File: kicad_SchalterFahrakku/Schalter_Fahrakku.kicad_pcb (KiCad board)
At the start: 2 copper layers, 10 parts, among them P3 uC_IN, Q1 IRLML6344, Q2 IPD90P03

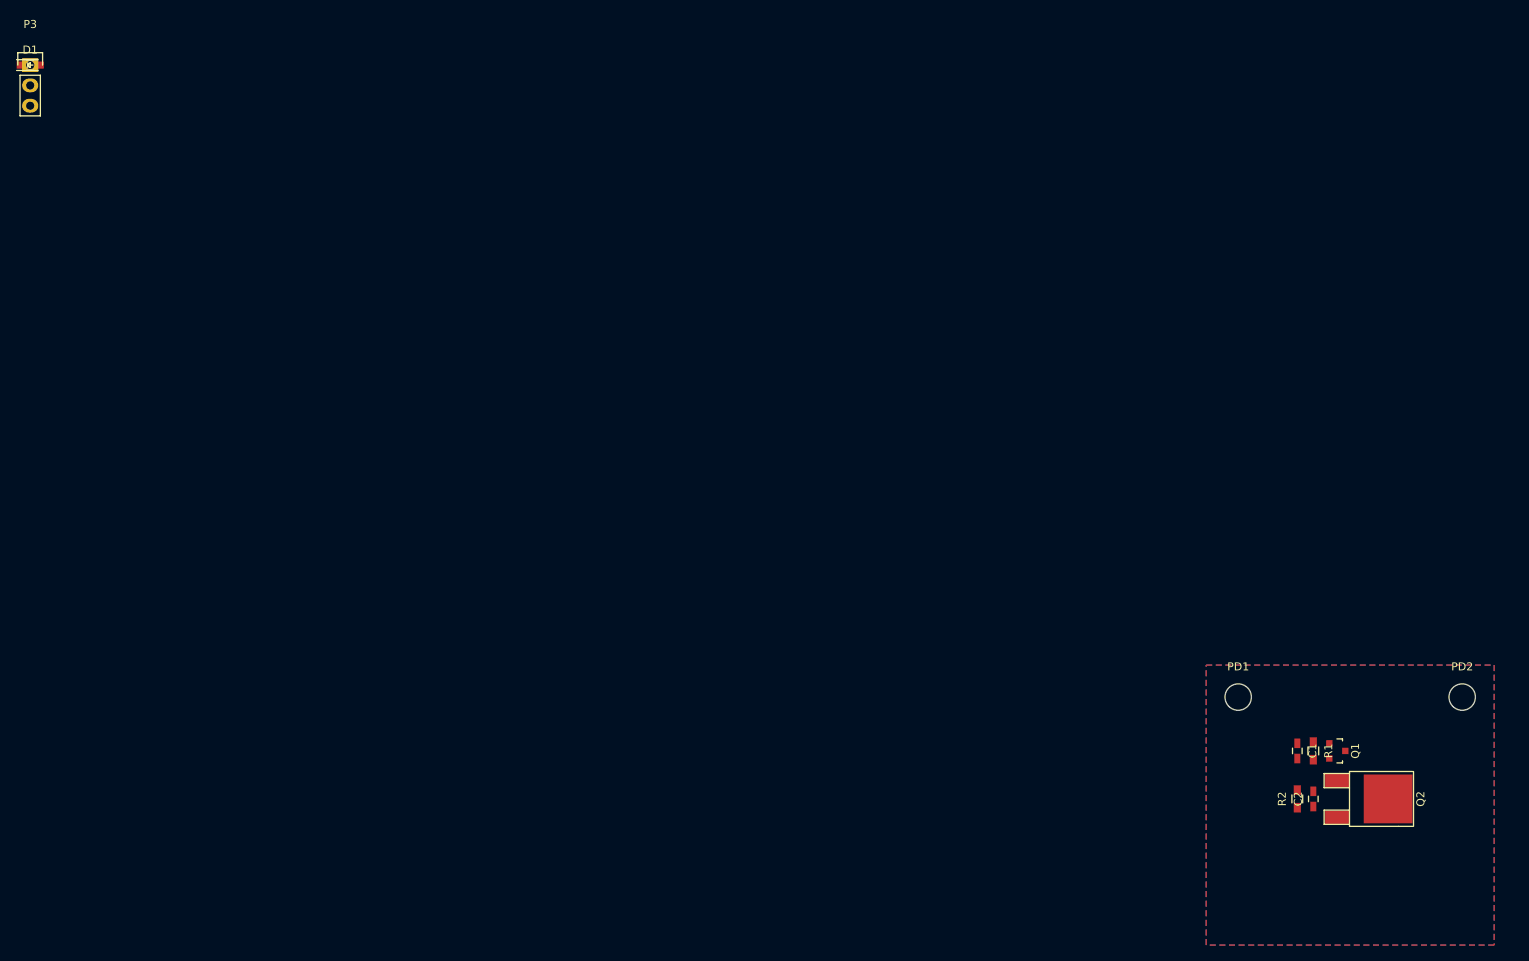
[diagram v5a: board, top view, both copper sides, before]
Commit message: - 5V_Servo Zusätzlich zur verfügung gestellt - Footprints für Pinleisten mit Verrigelung Hinzugefügt
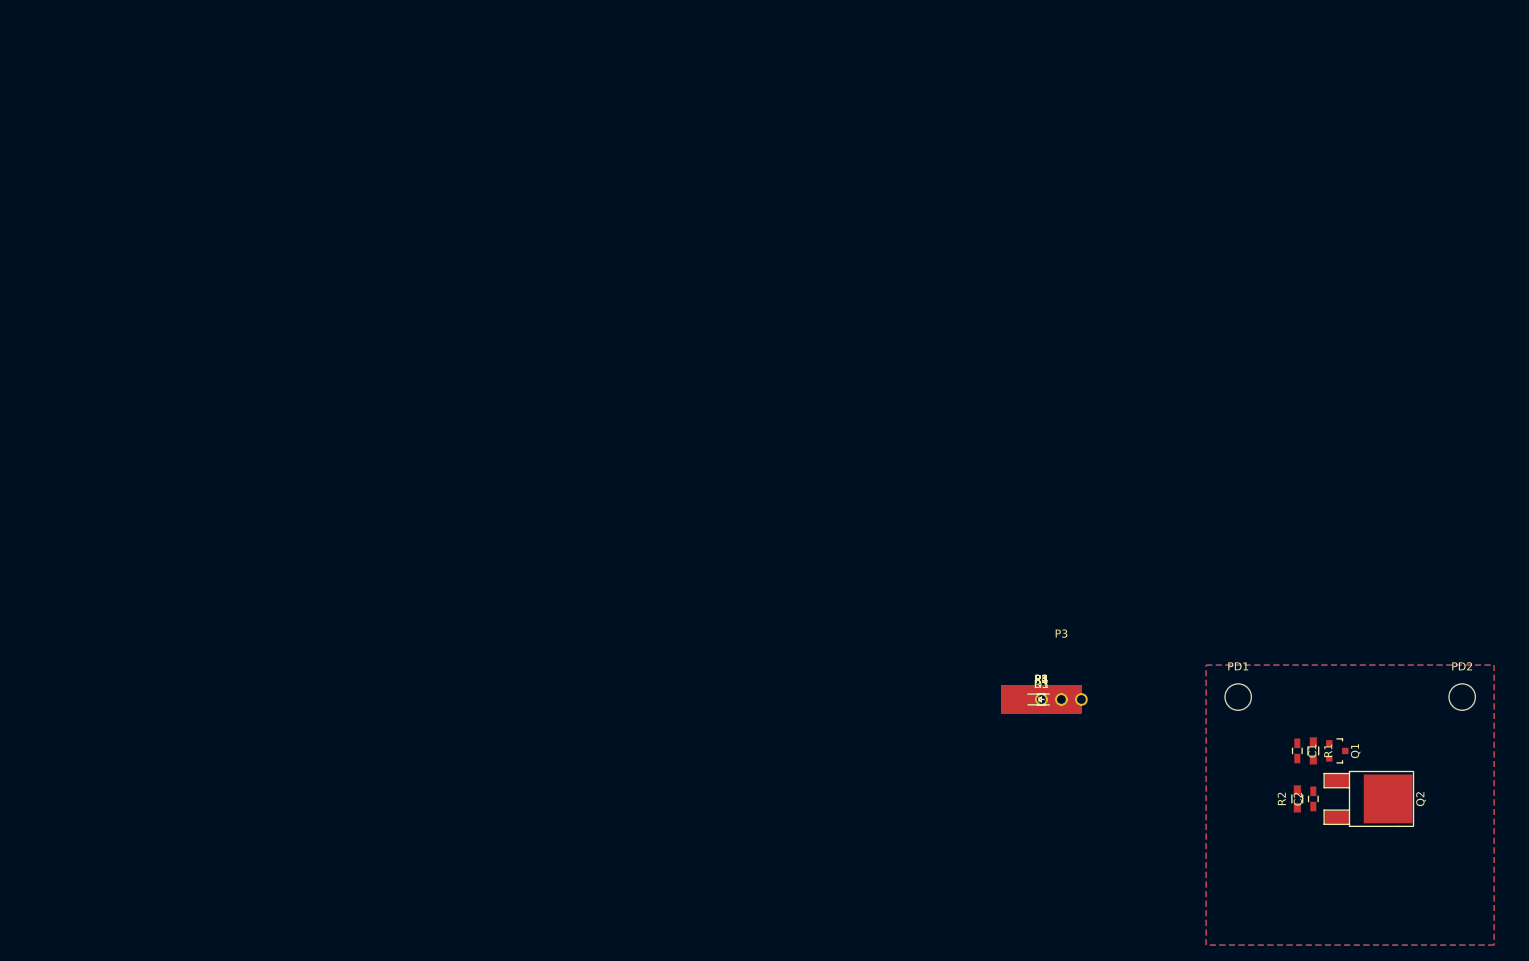
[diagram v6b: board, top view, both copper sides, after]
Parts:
- added P1: V_IN+, Custom:Pad_SMD_3.5x10, F.Cu at (126.4, 79.3)
- added P2: V_IN-, Custom:Pad_SMD_3.5x10, F.Cu at (126.4, 79.3)
- added P4, P5: V_OUT+, Custom:Pad_SMD_3.5x10, F.Cu at (126.4, 79.3)
- added R3: 3k6, Resistors_SMD:R_0603_HandSoldering, F.Cu at (126.4, 79.3)
- P3: footprint Pin_Headers:Pin_Header_Straight_1x03 -> Custom:PS25_3W_BR
- moved D1 149.2 mm to (126.4, 79.3)
- moved P3 149.2 mm to (126.4, 79.3)
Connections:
- D1 pad 2: (no net) -> Net-(D1-Pad2)
- Q2 pad 2: (no net) -> Net-(P4-Pad1)
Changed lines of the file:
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@@
 (kicad_pcb (version 4) (host pcbnew 4.0.2-stable)
   (general
-    (links 15)
-    (no_connects 13)
+    (links 19)
+    (no_connects 11)
     (area 0 0 0 0)
     (thickness 1.6)
@@
     (tracks 0)
     (zones 0)
-    (modules 10)
-    (nets 5)
+    (modules 15)
+    (nets 7)
   )
   (page A4)
@@
   (net 3 "Net-(C2-Pad1)")
   (net 4 "Net-(C2-Pad2)")
+  (net 5 "Net-(D1-Pad2)")
+  (net 6 "Net-(P4-Pad1)")
   (net_class Default "Dies ist die voreingestellte Netzklasse."
     (clearance 0.2)
@@
     (add_net "Net-(C2-Pad1)")
     (add_net "Net-(C2-Pad2)")
+    (add_net "Net-(D1-Pad2)")
+    (add_net "Net-(P4-Pad1)")
   )
   (module Capacitors_SMD:C_0603_HandSoldering (layer F.Cu)
@@
     (pad 1 smd rect (at -2.286 0 270) (size 1.651 3.048) (layers F.Cu F.Paste F.Mask)
       (net 4 "Net-(C2-Pad2)"))
-    (pad 2 smd rect (at 0 -6.35 270) (size 6.096 6.096) (layers F.Cu F.Paste F.Mask))
+    (pad 2 smd rect (at 0 -6.35 270) (size 6.096 6.096) (layers F.Cu F.Paste F.Mask)
+      (net 6 "Net-(P4-Pad1)"))
     (pad 3 smd rect (at 2.286 0 270) (size 1.651 3.048) (layers F.Cu F.Paste F.Mask)
       (net 3 "Net-(C2-Pad1)"))
@@
   )
   (module Custom:LED_0603_HandSoldering (layer F.Cu)
-    (at 0 0)
+    (at 126.4 79.3)
     (descr "Resistor SMD 0603, hand soldering")
     (tags "resistor 0603")
@@
     (pad 1 smd rect (at -1.1 0) (size 1.2 0.9) (layers F.Cu F.Paste F.Mask)
       (net 2 GND))
-    (pad 2 smd rect (at 1.1 0) (size 1.2 0.9) (layers F.Cu F.Paste F.Mask))
+    (pad 2 smd rect (at 1.1 0) (size 1.2 0.9) (layers F.Cu F.Paste F.Mask)
+      (net 5 "Net-(D1-Pad2)"))
     (model Resistors_SMD.3dshapes/R_0603_HandSoldering.wrl
       (at (xyz 0 0 0))
@@
     )
   )
-  (module Pin_Headers:Pin_Header_Straight_1x03 (layer F.Cu)
-    (at 0 0)
-    (descr "Through hole pin header")
-    (tags "pin header")
-    (fp_text reference P3 (at 0 -5.1) (layer F.SilkS)
-      (effects (font (size 1 1) (thickness 0.15)))
-    )
-    (fp_text value uC_IN (at 0 -3.1) (layer F.Fab)
-      (effects (font (size 1 1) (thickness 0.15)))
-    )
-    (fp_line (start -1.75 -1.75) (end -1.75 6.85) (layer F.CrtYd) (width 0.05))
-    (fp_line (start 1.75 -1.75) (end 1.75 6.85) (layer F.CrtYd) (width 0.05))
-    (fp_line (start -1.75 -1.75) (end 1.75 -1.75) (layer F.CrtYd) (width 0.05))
-    (fp_line (start -1.75 6.85) (end 1.75 6.85) (layer F.CrtYd) (width 0.05))
-    (fp_line (start -1.27 1.27) (end -1.27 6.35) (layer F.SilkS) (width 0.15))
-    (fp_line (start -1.27 6.35) (end 1.27 6.35) (layer F.SilkS) (width 0.15))
-    (fp_line (start 1.27 6.35) (end 1.27 1.27) (layer F.SilkS) (width 0.15))
-    (fp_line (start 1.55 -1.55) (end 1.55 0) (layer F.SilkS) (width 0.15))
-    (fp_line (start 1.27 1.27) (end -1.27 1.27) (layer F.SilkS) (width 0.15))
-    (fp_line (start -1.55 0) (end -1.55 -1.55) (layer F.SilkS) (width 0.15))
-    (fp_line (start -1.55 -1.55) (end 1.55 -1.55) (layer F.SilkS) (width 0.15))
-    (pad 1 thru_hole rect (at 0 0) (size 2.032 1.7272) (drill 1.016) (layers *.Cu *.Mask F.SilkS)
+  (module Custom:Pad_SMD_3.5x10 (layer F.Cu)
+    (at 126.4 79.3)
+    (fp_text reference P1 (at 0 -2.54 180) (layer F.SilkS)
+      (effects (font (size 1 1) (thickness 0.15)))
+    )
+    (fp_text value V_IN+ (at -0.0254 2.794) (layer F.Fab)
+      (effects (font (size 1 1) (thickness 0.15)))
+    )
+    (pad 1 smd rect (at 0 0) (size 10 3.5) (layers F.Cu F.Paste F.Mask)
       (net 3 "Net-(C2-Pad1)"))
-    (pad 2 thru_hole oval (at 0 2.54) (size 2.032 1.7272) (drill 1.016) (layers *.Cu *.Mask F.SilkS)
-      (net 2 GND))
-    (pad 3 thru_hole oval (at 0 5.08) (size 2.032 1.7272) (drill 1.016) (layers *.Cu *.Mask F.SilkS)
+  )
+  (module Custom:Pad_SMD_3.5x10 (layer F.Cu)
+    (at 126.4 79.3)
+    (fp_text reference P2 (at 0 -2.54 180) (layer F.SilkS)
+      (effects (font (size 1 1) (thickness 0.15)))
+    )
+    (fp_text value V_IN- (at -0.0254 2.794) (layer F.Fab)
+      (effects (font (size 1 1) (thickness 0.15)))
+    )
+    (pad 1 smd rect (at 0 0) (size 10 3.5) (layers F.Cu F.Paste F.Mask)
+      (net 2 GND))
+  )
+  (module Custom:PS25_3W_BR (layer F.Cu)
+    (at 126.4 79.3)
+    (fp_text reference P3 (at 2.5 -8.2) (layer F.SilkS)
+      (effects (font (size 1 1) (thickness 0.15)))
+    )
+    (fp_text value uC_IN (at 2.5 3.3) (layer F.Fab)
+      (effects (font (size 1 1) (thickness 0.15)))
+    )
+    (fp_line (start 6.5 -7.35) (end 6.5 -2.35) (layer F.CrtYd) (width 0.15))
+    (fp_line (start -1.5 -7.35) (end 6.5 -7.35) (layer F.CrtYd) (width 0.15))
+    (fp_line (start -1.5 -2.35) (end -1.5 -7.35) (layer F.CrtYd) (width 0.15))
+    (fp_line (start 6.5 2.35) (end -1.5 2.35) (layer F.CrtYd) (width 0.15))
+    (fp_line (start 6.5 -2.35) (end 6.5 2.35) (layer F.CrtYd) (width 0.15))
+    (fp_line (start -1.5 -2.35) (end 6.5 -2.35) (layer F.CrtYd) (width 0.15))
+    (fp_line (start -1.5 2.35) (end -1.5 -2.35) (layer F.CrtYd) (width 0.15))
+    (pad 1 thru_hole circle (at 0 0) (size 1.6 1.6) (drill 1.1) (layers *.Cu *.Mask F.SilkS)
+      (net 3 "Net-(C2-Pad1)"))
+    (pad 2 thru_hole circle (at 2.5 0) (size 1.6 1.6) (drill 1.1) (layers *.Cu *.Mask F.SilkS)
+      (net 2 GND))
+    (pad 3 thru_hole circle (at 5 0) (size 1.6 1.6) (drill 1.1) (layers *.Cu *.Mask F.SilkS)
       (net 1 /CTL_DRIVE))
-    (model Pin_Headers.3dshapes/Pin_Header_Straight_1x03.wrl
-      (at (xyz 0 -0.1 0))
-      (scale (xyz 1 1 1))
-      (rotate (xyz 0 0 90))
-    )
-  )
+  )
+  (module Custom:Pad_SMD_3.5x10 (layer F.Cu)
+    (at 126.4 79.3)
+    (fp_text reference P4 (at 0 -2.54 180) (layer F.SilkS)
+      (effects (font (size 1 1) (thickness 0.15)))
+    )
+    (fp_text value V_OUT+ (at -0.0254 2.794) (layer F.Fab)
+      (effects (font (size 1 1) (thickness 0.15)))
+    )
+    (pad 1 smd rect (at 0 0) (size 10 3.5) (layers F.Cu F.Paste F.Mask)
+      (net 6 "Net-(P4-Pad1)"))
+  )
+  (module Custom:Pad_SMD_3.5x10 (layer F.Cu)
+    (at 126.4 79.3)
+    (fp_text reference P5 (at 0 -2.54 180) (layer F.SilkS)
+      (effects (font (size 1 1) (thickness 0.15)))
+    )
+    (fp_text value V_OUT+ (at -0.0254 2.794) (layer F.Fab)
+      (effects (font (size 1 1) (thickness 0.15)))
+    )
+    (pad 1 smd rect (at 0 0) (size 10 3.5) (layers F.Cu F.Paste F.Mask)
+      (net 2 GND))
+  )
+  (module Resistors_SMD:R_0603_HandSoldering (layer F.Cu)
+    (at 126.4 79.3)
+    (descr "Resistor SMD 0603, hand soldering")
+    (tags "resistor 0603")
+    (attr smd)
+    (fp_text reference R3 (at 0 -1.9) (layer F.SilkS)
+      (effects (font (size 1 1) (thickness 0.15)))
+    )
+    (fp_text value 3k6 (at 0 1.9) (layer F.Fab)
+      (effects (font (size 1 1) (thickness 0.15)))
+    )
+    (fp_line (start -2 -0.8) (end 2 -0.8) (layer F.CrtYd) (width 0.05))
+    (fp_line (start -2 0.8) (end 2 0.8) (layer F.CrtYd) (width 0.05))
+    (fp_line (start -2 -0.8) (end -2 0.8) (layer F.CrtYd) (width 0.05))
+    (fp_line (start 2 -0.8) (end 2 0.8) (layer F.CrtYd) (width 0.05))
+    (fp_line (start 0.5 0.675) (end -0.5 0.675) (layer F.SilkS) (width 0.15))
+    (fp_line (start -0.5 -0.675) (end 0.5 -0.675) (layer F.SilkS) (width 0.15))
+    (pad 1 smd rect (at -1.1 0) (size 1.2 0.9) (layers F.Cu F.Paste F.Mask)
+      (net 6 "Net-(P4-Pad1)"))
+    (pad 2 smd rect (at 1.1 0) (size 1.2 0.9) (layers F.Cu F.Paste F.Mask)
+      (net 5 "Net-(D1-Pad2)"))
+    (model Resistors_SMD.3dshapes/R_0603_HandSoldering.wrl
+      (at (xyz 0 0 0))
+      (scale (xyz 1 1 1))
+      (rotate (xyz 0 0 0))
+    )
+  )

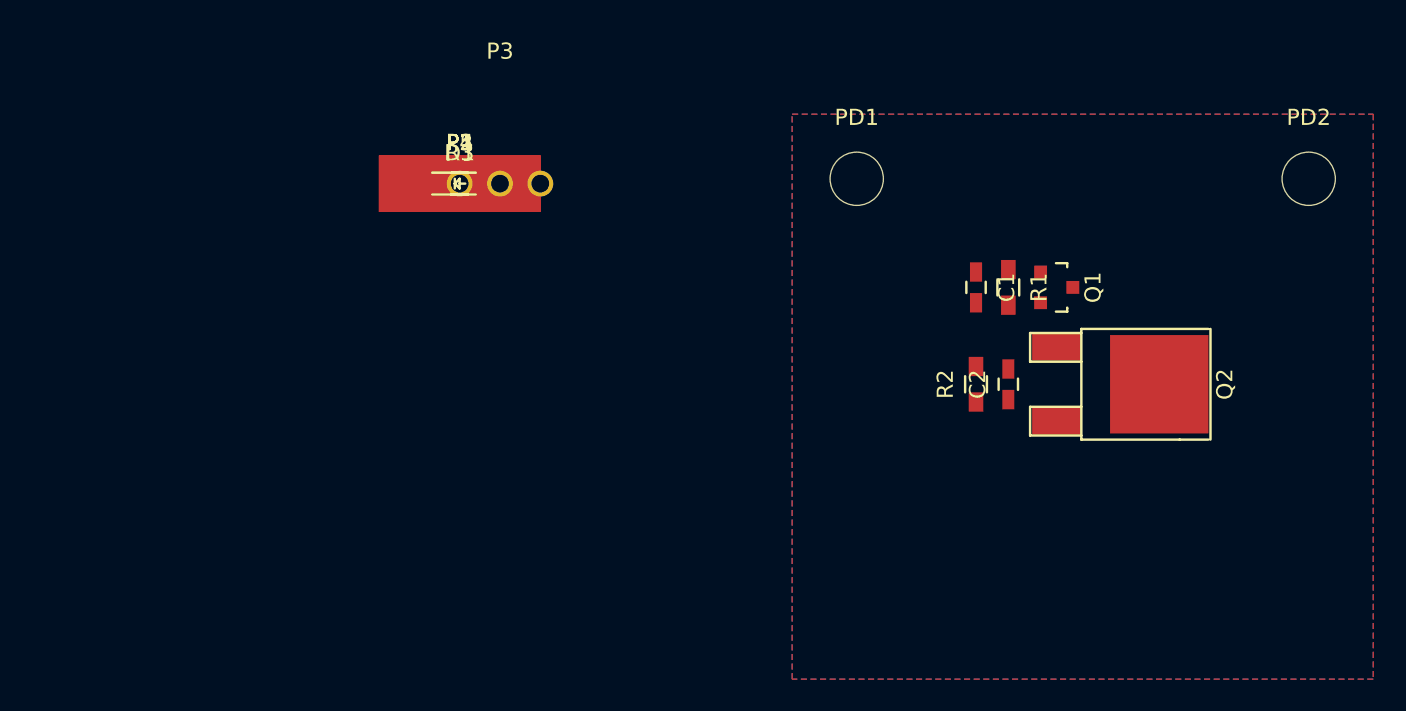
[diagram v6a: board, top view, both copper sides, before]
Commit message: - Layout Schalterplatine ohne Routing
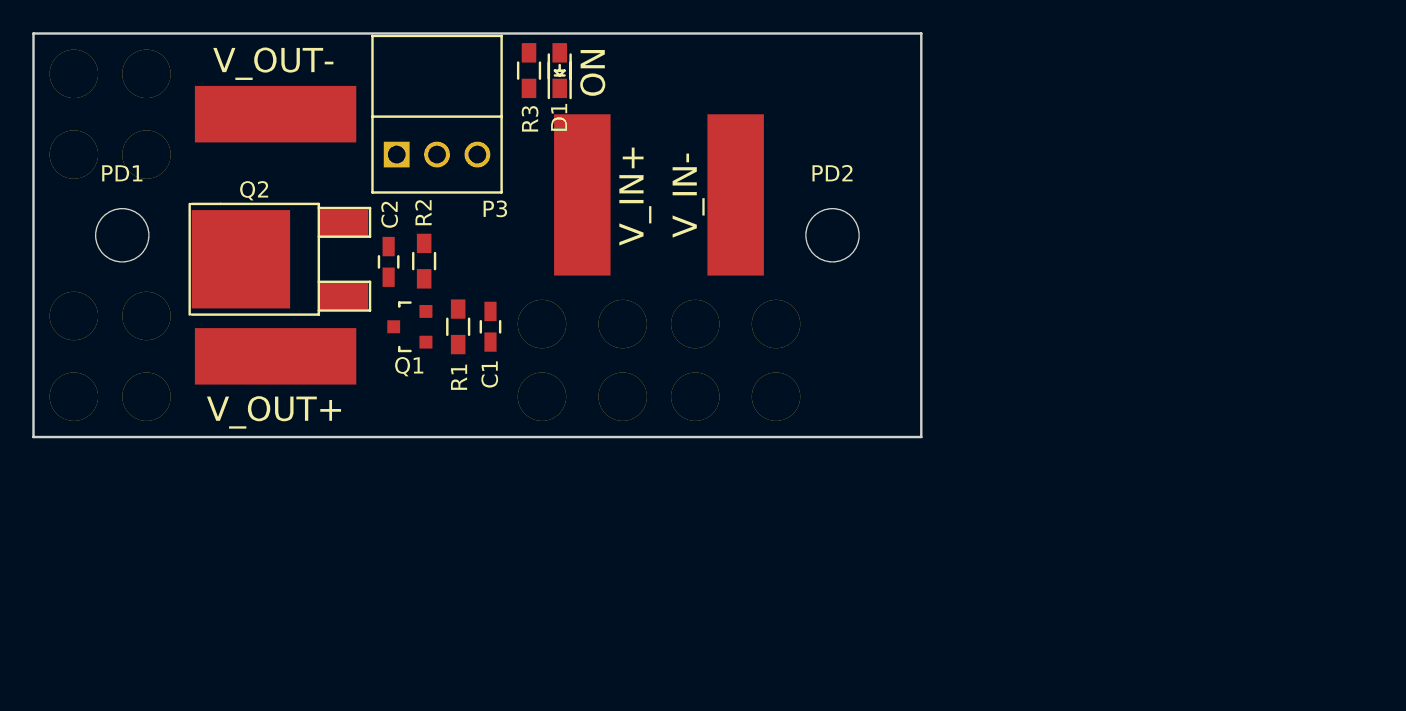
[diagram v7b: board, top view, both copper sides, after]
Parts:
- added PD10: Hole, Custom:Hole_3mm, F.Cu at (107.0, 72.5)
- added PD11: Hole, Custom:Hole_3mm, F.Cu at (131.5, 92.5)
- added PD12: Hole, Custom:Hole_3mm, F.Cu at (136.5, 92.5)
- added PD13: Hole, Custom:Hole_3mm, F.Cu at (131.5, 88.0)
- added PD14: Hole, Custom:Hole_3mm, F.Cu at (136.5, 88.0)
- added PD15: Hole, Custom:Hole_3mm, F.Cu at (146.0, 92.5)
- added PD16: Hole, Custom:Hole_3mm, F.Cu at (141.0, 92.5)
- added PD17: Hole, Custom:Hole_3mm, F.Cu at (141.0, 88.0)
- added PD18: Hole, Custom:Hole_3mm, F.Cu at (146.0, 88.0)
- added PD3: Hole, Custom:Hole_3mm, F.Cu at (102.5, 92.5)
- added PD4: Hole, Custom:Hole_3mm, F.Cu at (107.0, 92.5)
- added PD5: Hole, Custom:Hole_3mm, F.Cu at (102.5, 87.5)
- added PD6: Hole, Custom:Hole_3mm, F.Cu at (107.0, 87.5)
- added PD7: Hole, Custom:Hole_3mm, F.Cu at (102.5, 77.5)
- added PD8: Hole, Custom:Hole_3mm, F.Cu at (107.0, 77.5)
- added PD9: Hole, Custom:Hole_3mm, F.Cu at (102.5, 72.5)
- P3: footprint Custom:PS25_3W_BR -> Custom:PS25_3W
- P5: value V_OUT+ -> V_OUT-
- moved PD1 45.6 mm to (105.5, 82.5)
- moved Q2 44.9 mm to (119.2, 84.0), turned to 90 degrees
- moved Q1 40.2 mm to (123.3, 88.2), turned to 90 degrees
- moved C2 39.1 mm to (122.0, 84.2), turned to 270 degrees
- moved R2 35.0 mm to (124.2, 84.1), turned to 270 degrees
- moved R1 34.2 mm to (126.3, 88.2), turned to 90 degrees
- moved C1 30.2 mm to (128.3, 88.2), turned to 90 degrees
- moved PD2 29.7 mm to (149.5, 82.5)
- moved P2 17.1 mm to (143.5, 80.0), turned to 90 degrees
- moved P4 15.6 mm to (115.0, 90.0)
- moved P5 12.2 mm to (115.0, 75.0)
- moved D1 9.35 mm to (132.6, 72.3), turned to 90 degrees
- moved R3 8.22 mm to (130.7, 72.3), turned to 90 degrees
- moved P1 7.63 mm to (134.0, 80.0), turned to 90 degrees
- moved P3 4.30 mm to (122.5, 77.5)
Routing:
- removed copper zone on B.Cu, net GND
- removed copper zone on F.Cu, net GND
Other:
- board outline added: 55 x 25 mm
- board text added: "ON"
- board text added: "V_IN+"
- board text added: "V_IN-"
- board text added: "V_OUT+"
- board text added: "V_OUT-"
